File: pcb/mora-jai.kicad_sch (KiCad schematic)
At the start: 28 parts, among them J1 Conn_01x02, J2 Conn_01x04, J3 Conn_01x02, J4 Conn_01x01, J5 Conn_01x03, SW1 SW_Push, SW10 SW_Push, SW11 SW_Push, SW12 SW_Push, SW13 SW_Push, SW14 SW_Push, SW15 SW_Push, SW16 SW_Push, SW2 SW_Push, SW3 SW_Push, SW4 SW_Push, SW5 SW_Push, SW6 SW_Push, SW7 SW_Push, SW8 SW_Push, SW9 SW_Push, U1 CD74HC4067M, U3 XIAO-ESP32-S3-SMD

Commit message: add notes to PCB and schematic for revision 2
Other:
- note added: "TODO: - Add battery charging circuit - Add +BATT -> +5V boost converter circuit - Add MOSFET to cut off +BATT output when VBUS is connected"
- note added: "VBUS"
- note added: "battery"
- note added: "battery charger"
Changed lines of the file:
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@@
+	)
+	(rectangle
+		(start 158.496 124.46)
+		(end 173.482 134.366)
+		(stroke
+			(width 0)
+			(type default)
+		)
+		(fill
+			(type none)
+		)
+	)
+	(rectangle
+		(start 179.07 125.476)
+		(end 194.056 135.382)
+		(stroke
+			(width 0)
+			(type default)
+		)
+		(fill
+			(type none)
+		)
+	)
+	(rectangle
+		(start 157.734 144.526)
+		(end 172.72 154.432)
+		(stroke
+			(width 0)
+			(type default)
+		)
+		(fill
+			(type none)
+		)
 	)
 	(rectangle
@@
 		(fill
 			(type none)
+		)
+	)
+	(text "TODO:\n- Add battery charging circuit\n- Add +BATT -> +5V boost converter circuit\n- Add MOSFET to cut off +BATT output when VBUS is connected\n"
+		(exclude_from_sim no)
+		(at 191.77 147.066 0)
+		(effects
+			(font
+				(size 1.27 1.27)
+			)
+			(justify left)
+		)
+	)
+	(text "battery\ncharger"
+		(exclude_from_sim no)
+		(at 165.1 129.286 0)
+		(effects
+			(font
+				(size 1.27 1.27)
+			)
 		)
 	)
@@
 		)
 	)
+	(text "VBUS"
+		(exclude_from_sim no)
+		(at 164.338 149.352 0)
+		(effects
+			(font
+				(size 1.27 1.27)
+			)
+		)
+	)
+	(text "battery"
+		(exclude_from_sim no)
+		(at 185.674 130.302 0)
+		(effects
+			(font
+				(size 1.27 1.27)
+			)
+		)
+	)
 	(text "5V Servo connector"
 		(exclude_from_sim no)
@@
 		)
 	)
+	(polyline
+		(pts
+			(xy 166.116 133.858) (xy 166.116 135.636)
+		)
+		(stroke
+			(width 0)
+			(type default)
+		)
+	)
 	(wire
 		(pts
@@
 		)
 		(stroke
+			(width 0)
+			(type default)
+		)
+	)
+	(polyline
+		(pts
+			(xy 166.37 144.526) (xy 166.37 135.636)
+		)
+		(stroke
+			(width 0)
+			(type default)
+		)
+	)
+	(polyline
+		(pts
+			(xy 166.37 135.636) (xy 166.116 135.636)
+		)
+		(stroke

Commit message: add a note and clean up schematic, last commit of rev. 1
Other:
- note added: "TODO: - Add battery charging circuit - Add +BATT -> +5V boost converter circuit - Add MOSFET to cut off +BATT output when VBUS is connected - DECOUPLING CAPACITORS!!!!"
- note removed: "TODO: - Add battery charging circuit - Add +BATT -> +5V boost converter circuit - Add MOSFET to cut off +BATT output when VBUS is connected"
- note removed: "VBUS"
- note removed: "battery"
- note removed: "battery charger"
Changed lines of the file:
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@@
-	)
-	(rectangle
-		(start 158.496 124.46)
-		(end 173.482 134.366)
-		(stroke
-			(width 0)
-			(type default)
-		)
-		(fill
-			(type none)
-		)
-	)
-	(rectangle
-		(start 179.07 125.476)
-		(end 194.056 135.382)
-		(stroke
-			(width 0)
-			(type default)
-		)
-		(fill
-			(type none)
-		)
-	)
-	(rectangle
-		(start 157.734 144.526)
-		(end 172.72 154.432)
-		(stroke
-			(width 0)
-			(type default)
-		)
-		(fill
-			(type none)
-		)
 	)
 	(rectangle
@@
 		)
 	)
-	(text "TODO:\n- Add battery charging circuit\n- Add +BATT -> +5V boost converter circuit\n- Add MOSFET to cut off +BATT output when VBUS is connected\n"
+	(text "TODO:\n- Add battery charging circuit\n- Add +BATT -> +5V boost converter circuit\n- Add MOSFET to cut off +BATT output when VBUS is connected\n- DECOUPLING CAPACITORS!!!!\n\n"
 		(exclude_from_sim no)
-		(at 191.77 147.066 0)
+		(at 214.122 144.78 0)
 		(effects
 			(font
@@
 			)
 			(justify left)
-		)
-	)
-	(text "battery\ncharger"
-		(exclude_from_sim no)
-		(at 165.1 129.286 0)
-		(effects
-			(font
-				(size 1.27 1.27)
-			)
 		)
 	)
@@
 		)
 	)
-	(text "VBUS"
-		(exclude_from_sim no)
-		(at 164.338 149.352 0)
-		(effects
-			(font
-				(size 1.27 1.27)
-			)
-		)
-	)
-	(text "battery"
-		(exclude_from_sim no)
-		(at 185.674 130.302 0)
-		(effects
-			(font
-				(size 1.27 1.27)
-			)
-		)
-	)
 	(text "5V Servo connector"
 		(exclude_from_sim no)
@@
 		)
 	)
-	(polyline
-		(pts
-			(xy 166.116 133.858) (xy 166.116 135.636)
-		)
-		(stroke
-			(width 0)
-			(type default)
-		)
-	)
 	(wire
 		(pts
@@
 		)
 		(stroke
-			(width 0)
-			(type default)
-		)
-	)
-	(polyline
-		(pts
-			(xy 166.37 144.526) (xy 166.37 135.636)
-		)
-		(stroke
-			(width 0)
-			(type default)
-		)
-	)
-	(polyline
-		(pts
-			(xy 166.37 135.636) (xy 166.116 135.636)
-		)
-		(stroke

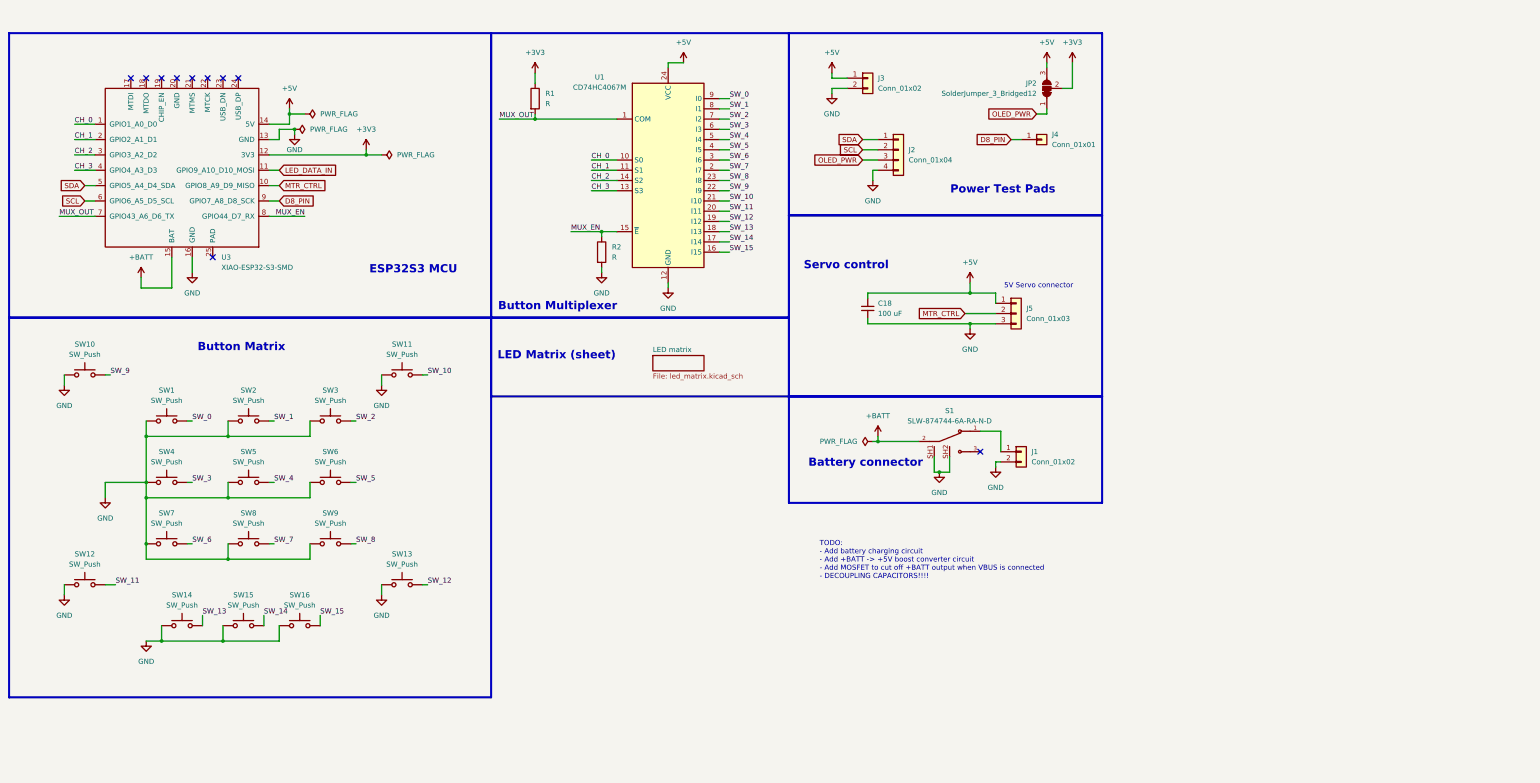
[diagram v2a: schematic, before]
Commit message: added mounting holes, 3.5mm diameter
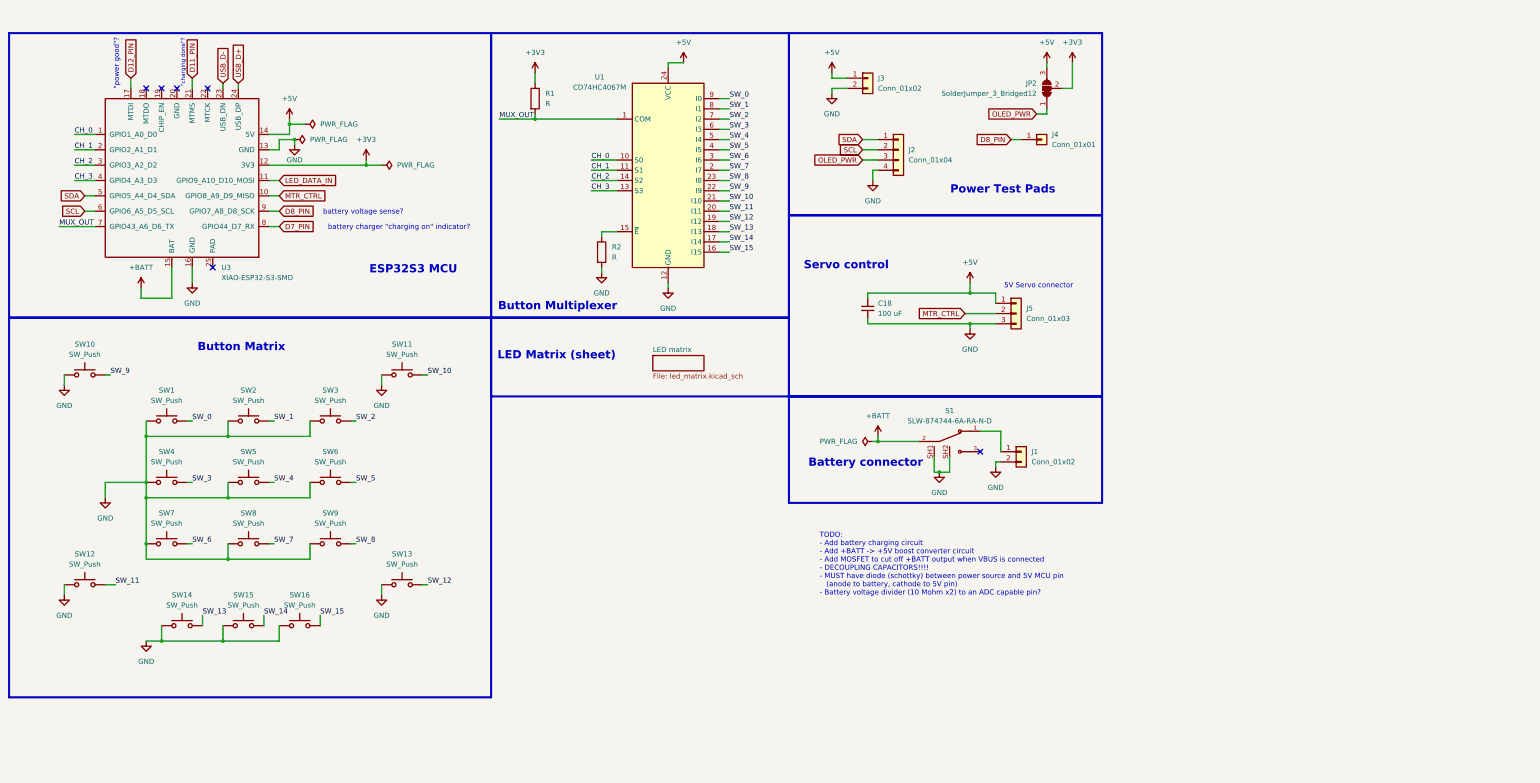
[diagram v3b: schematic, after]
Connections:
- net D12_PIN: now reaches U3.17 (MTDI)
- net D11_PIN: now reaches U3.21 (MTMS)
- net USB_D-: now reaches U3.23 (USB_DN)
- net USB_D+: now reaches U3.24 (USB_DP)
- net MUX_EN: no longer names the net of R2.1, U1.15 (~{E})
- net MUX_EN: no longer U3.8 (GPIO44_D7_RX)
- new net D7_PIN: U3.8 (GPIO44_D7_RX)
- no-connect marks 10 -> 6
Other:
- note added: ""charging done"?"
- note added: ""power good"?"
- note added: "TODO: - Add battery charging circuit - Add +BATT -> +5V boost converter circuit - Add MOSFET to cut off +BATT output when VBUS is connected - DECOUPLING CAPACITORS!!!! - MUST have diode (schottky) between power source and 5V MCU pin (anode to battery, cathode to 5V pin) - Battery voltage divider (10 Mohm x2) to an ADC capable pin?"
- note added: "battery charger "charging on" indicator?"
- note added: "battery voltage sense?"
- note removed: "TODO: - Add battery charging circuit - Add +BATT -> +5V boost converter circuit - Add MOSFET to cut off +BATT output when VBUS is connected - DECOUPLING CAPACITORS!!!!"
- moved on the sheet: U3

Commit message: added battery charger circuit, needs a once-over
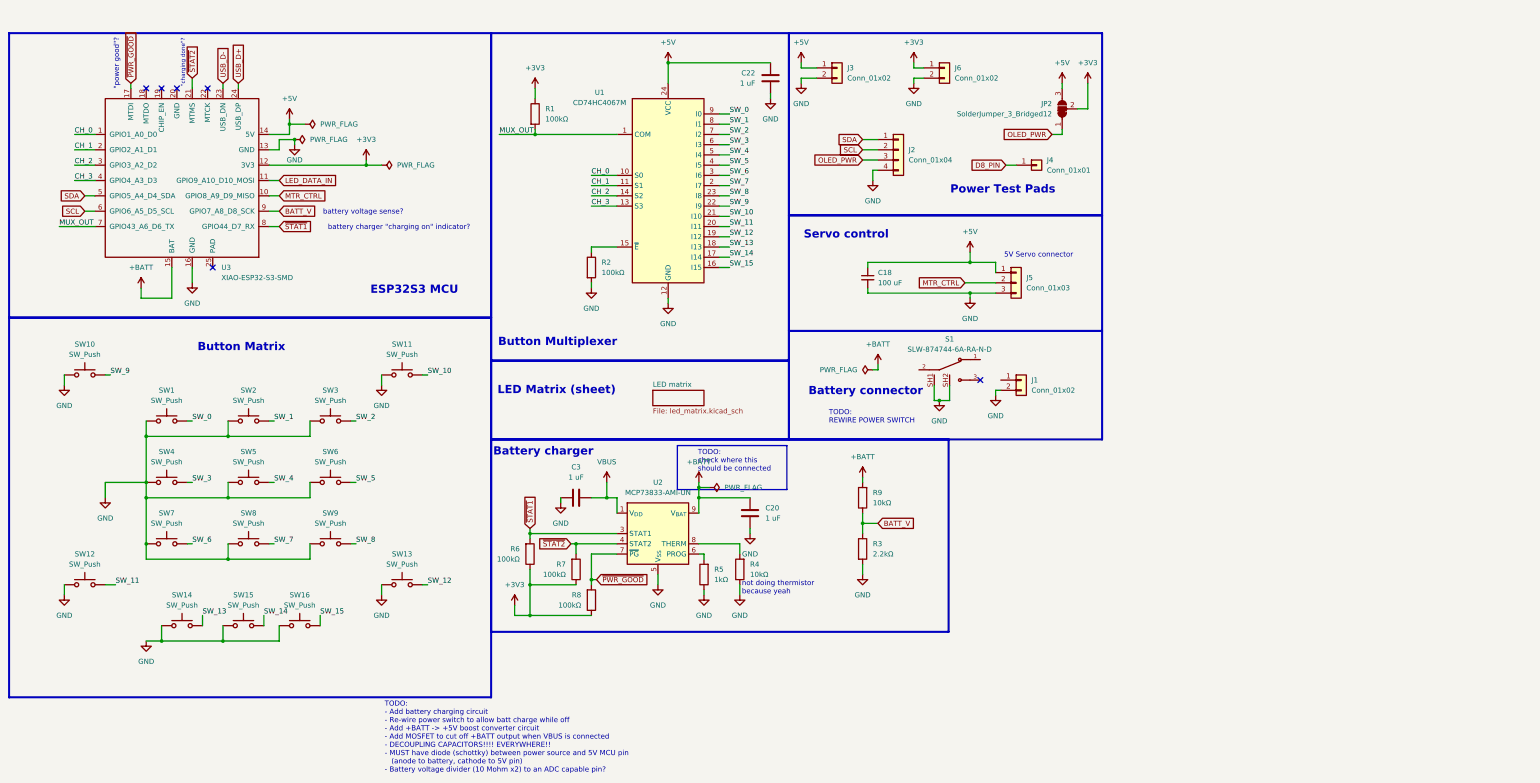
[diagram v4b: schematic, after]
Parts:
- added C20, C22, C3: 1 uF, symbol Device:C
- added J6: Conn_01x02, Connector_PinSocket_2.54mm:PinSocket_1x02_P2.54mm_Vertical, symbol Connector_Generic:Conn_01x02
- added R3: 2.2kΩ, symbol Device:R
- added R4, R9: 10kΩ, symbol Device:R
- added R5: 1kΩ, symbol Device:R
- added R6, R7, R8: 100kΩ, symbol Device:R
- added U2: MCP73833-AMI-UN, Package_SO:MSOP-10_3x3mm_P0.5mm, symbol Battery_Management:MCP73833-xxx-UN
- R1, R2: value R -> 100kΩ
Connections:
- net +3V3: now also J6.1 (Pin_1), R6.1, R7.1, R8.1
- net +5V: now also C22.2
- net +BATT: now also C20.1, R9.2, U2.10 (V_{BAT}), U2.9 (V_{BAT}); no longer S1.2
- net D8_PIN: no longer U3.9 (GPIO7_A8_D8_SCK)
- net GND: now also C20.2, C22.1, C3.1, J6.2 (Pin_2), R3.2, R4.1, R5.1, U2.5 (V_{SS})
- net at J1.1 (Pin_1): no longer S1.1
- net D11_PIN renamed ~{STAT2}
- net ~{STAT2}: now also R7.2, U2.4 (STAT2)
- net D12_PIN renamed ~{PWR_GOOD}
- net ~{PWR_GOOD}: now also R8.2, U2.7 (~{PG})
- net D7_PIN renamed ~{STAT1}
- net ~{STAT1}: now also R6.2, U2.3 (STAT1)
- new net: R5.2, U2.6 (PROG)
- new net: R4.2, U2.8 (THERM)
- new net BATT_V: R3.1, R9.1, U3.9 (GPIO7_A8_D8_SCK)
- new net VBUS: C3.2, U2.1 (V_{DD}), U2.2 (V_{DD})
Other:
- note added: "Battery charger"
- note added: "TODO: - Add battery charging circuit - Re-wire power switch to allow batt charge while off - Add +BATT -> +5V boost converter circuit - Add MOSFET to cut off +BATT output when VBUS is connected - DECOUPLING CAPACITORS!!!! EVERYWHERE!! - MUST have diode (schottky) between power source and 5V MCU pin (anode to battery, cathode to 5V pin) - Battery voltage divider (10 Mohm x2) to an ADC capable pin?"
- note added: "TODO: REWIRE POWER SWITCH"
- note added: "TODO: check where this should be connected"
- note added: "not doing thermistor because yeah"
- note removed: "TODO: - Add battery charging circuit - Add +BATT -> +5V boost converter circuit - Add MOSFET to cut off +BATT output when VBUS is connected - DECOUPLING CAPACITORS!!!! - MUST have diode (schottky) between power source and 5V MCU pin (anode to battery, cathode to 5V pin) - Battery voltage divider (10 Mohm x2) to an ADC capable pin?"
- moved on the sheet: C18, J1, J3, J4, J5, JP2, R1, R2, S1, U1

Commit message: finished (?) schematic for rev. 2 power circuits
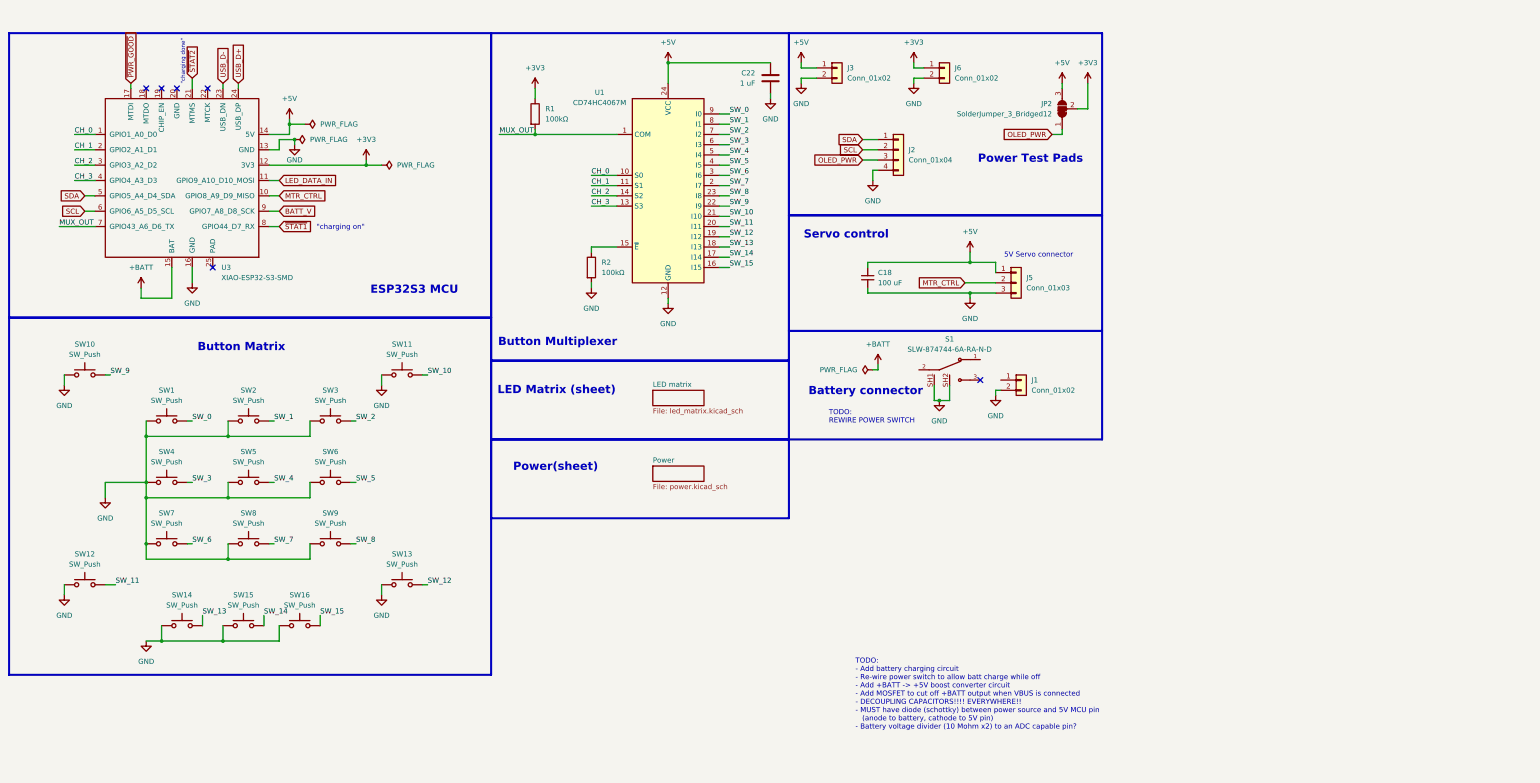
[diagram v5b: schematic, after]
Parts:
- removed C20, C3: 1 uF, symbol Device:C
- removed J4: Conn_01x01, Connector_PinHeader_2.54mm:PinHeader_1x01_P2.54mm_Vertical, symbol Connector_Generic:Conn_01x01
- removed R3: 2.2kΩ, symbol Device:R
- removed R4, R9: 10kΩ, symbol Device:R
- removed R5: 1kΩ, symbol Device:R
- removed R6, R7, R8: 100kΩ, symbol Device:R
- removed U2: MCP73833-AMI-UN, Package_SO:MSOP-10_3x3mm_P0.5mm, symbol Battery_Management:MCP73833-xxx-UN
- C22: footprint (none) -> Capacitor_SMD:C_0805_2012Metric_Pad1.18x1.45mm_HandSolder
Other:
- added sheet Power (power.kicad_sch)
- note added: ""charging done""
- note added: ""charging on""
- note added: "Power(sheet)"
- note removed: ""charging done"?"
- note removed: ""power good"?"
- note removed: "Battery charger"
- note removed: "TODO: check where this should be connected"
- note removed: "battery charger "charging on" indicator?"
- note removed: "battery voltage sense?"
- note removed: "not doing thermistor because yeah"

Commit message: placing power components
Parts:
- removed J1: Conn_01x02, Connector_JST:JST_PH_S2B-PH-K_1x02_P2.00mm_Horizontal, symbol Connector_Generic:Conn_01x02
- removed J3, J6: Conn_01x02, Connector_PinSocket_2.54mm:PinSocket_1x02_P2.54mm_Vertical, symbol Connector_Generic:Conn_01x02
- removed S1: SLW-874744-6A-RA-N-D, Mora_Jai_Parts:SW_SLW-874744-6A-RA-N-D, symbol Mora_Jai_Sym:SLW-874744-6A-RA-N-D
- added D18: D_Schottky, Diode_SMD:D_SOD-123F, symbol Device:D_Schottky
- added TP1: TestPoint, symbol Connector:TestPoint
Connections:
- net +5V: now also D18.2 (A); no longer U3.14 (5V)
- net GND: no longer U3.16 (GND)
- net +BATT: no longer names the net of U3.15 (BAT)
- new net: D18.1 (K), U3.14 (5V)
- no-connect marks 6 -> 5
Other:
- note added: "OLED display connector (I2C)"
- note added: "TODO: - CHECK DECOUPLING CAPACITORS!!!! EVERYWHERE!! - Edit footprint for MCU to expose other bottom pads - Expose more test pins/pads (all chip connectors)"
- note removed: "Battery connector"
- note removed: "Power Test Pads"
- note removed: "TODO: - Add battery charging circuit - Re-wire power switch to allow batt charge while off - Add +BATT -> +5V boost converter circuit - Add MOSFET to cut off +BATT output when VBUS is connected - DECOUPLING CAPACITORS!!!! EVERYWHERE!! - MUST have diode (schottky) between power source and 5V MCU pin (anode to battery, cathode to 5V pin) - Battery voltage divider (10 Mohm x2) to an ADC capable pin?"
- note removed: "TODO: REWIRE POWER SWITCH"
- moved on the sheet: C18, J2, J5, JP2

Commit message: power components all placed, added test pads for all MCU pins
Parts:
- added TP2, TP3, TP4, TP5, TP6: TestPoint, TestPoint:TestPoint_Pad_D2.5mm, symbol Connector:TestPoint
- TP1: footprint (none) -> TestPoint:TestPoint_Pad_D2.5mm
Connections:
- net BATT_V: now also TP5.1
- net GND: now also U3.16 (GND)
- net LED_DATA_IN: now also TP4.1
- net MTDO: now reaches TP1.1
- net MTDO: now also U3.18 (MTDO)
- net ESPBAT: now reaches U3.15 (BAT)
- net ESPBAT: now also TP6.1
- net CHIP_EN: now reaches U3.19 (CHIP_EN)
- net CHIP_EN: now also TP3.1
- net MTCK: now reaches U3.22 (MTCK)
- net MTCK: now also TP2.1
- no-connect marks 5 -> 2
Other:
- note added: "MCU test pads"
- moved on the sheet: TP1
